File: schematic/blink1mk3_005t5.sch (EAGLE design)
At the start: 18 parts, among them T0A TPTP15R, T1B TPTP15R, U1 EFM32HG309F64G, X1 USB

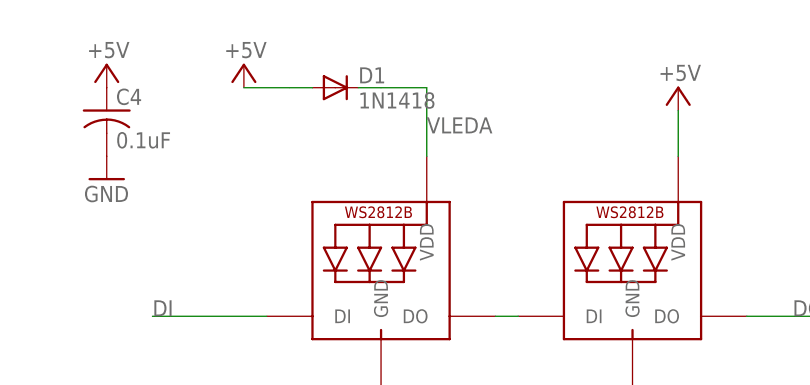
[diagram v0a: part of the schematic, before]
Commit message: schematic mk3_005t5, fix D1 part number
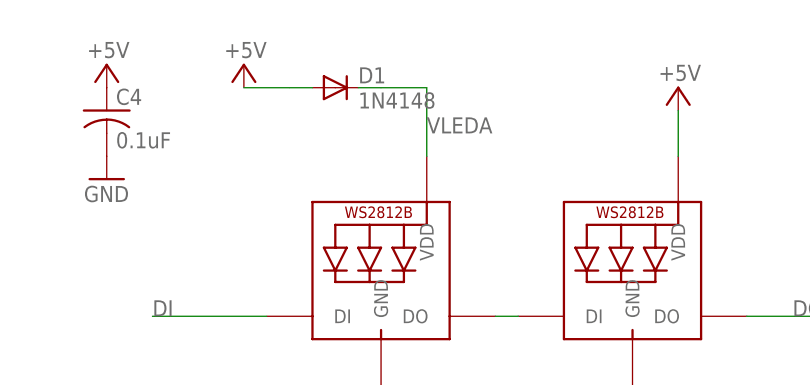
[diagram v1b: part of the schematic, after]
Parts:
- D1: value 1N1418 -> 1N4148
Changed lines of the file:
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@@
 <part name="P+2" library="supply1" deviceset="+5V" device=""/>
 <part name="GND3" library="supply1" library_urn="urn:adsk.eagle:library:371" deviceset="GND" device=""/>
-<part name="D1" library="diode" library_urn="urn:adsk.eagle:library:210" deviceset="DIODE-" device="SOD523" package3d_urn="urn:adsk.eagle:package:43410/1" value="1N1418"/>
+<part name="D1" library="diode" library_urn="urn:adsk.eagle:library:210" deviceset="DIODE-" device="SOD523" package3d_urn="urn:adsk.eagle:package:43410/1" value="1N4148"/>
 <part name="C4" library="adafruit" library_urn="urn:adsk.eagle:library:420" deviceset="C-US" device="C0402" value="0.1uF"/>
 <part name="P+3" library="supply1" deviceset="+5V" device=""/>
